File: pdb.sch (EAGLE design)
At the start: 35 parts, among them Q1 20MHz, Q2 IRFR5305PBF, Q3 IRFR5305PBF, U1 TSR_1-2433, U2 LTC2946CMSPBF, U3 LTC2946CMSPBF, U4 LTC2946CMSPBF, U5 ATMEGA48-20AU, U6 TXB0104

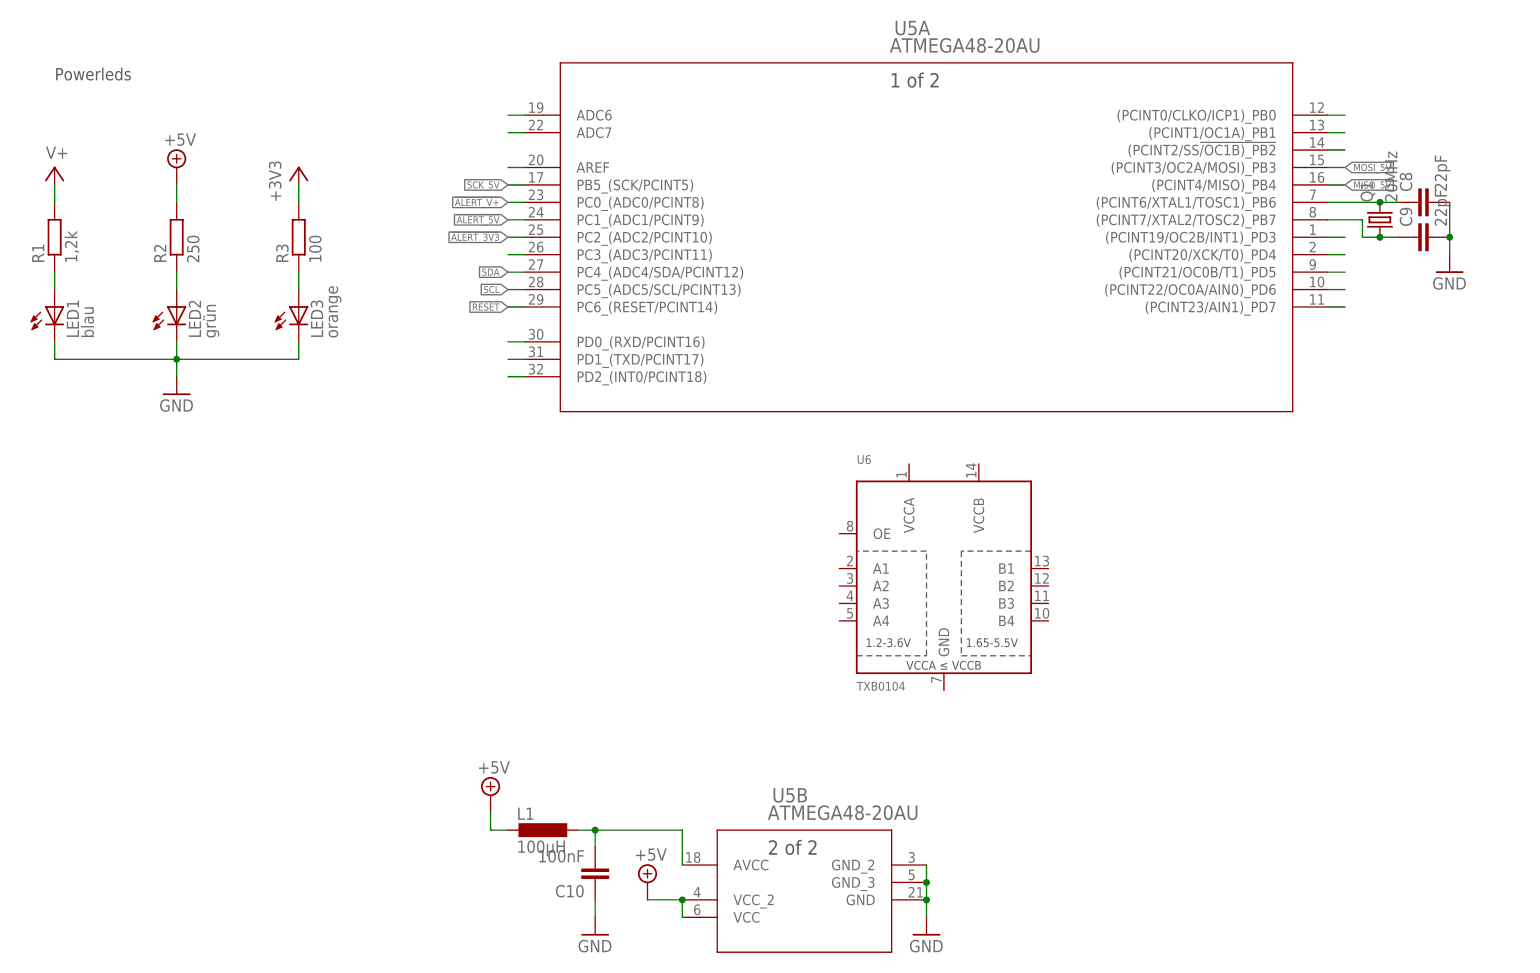
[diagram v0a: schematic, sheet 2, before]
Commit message: Connected Levelshifter
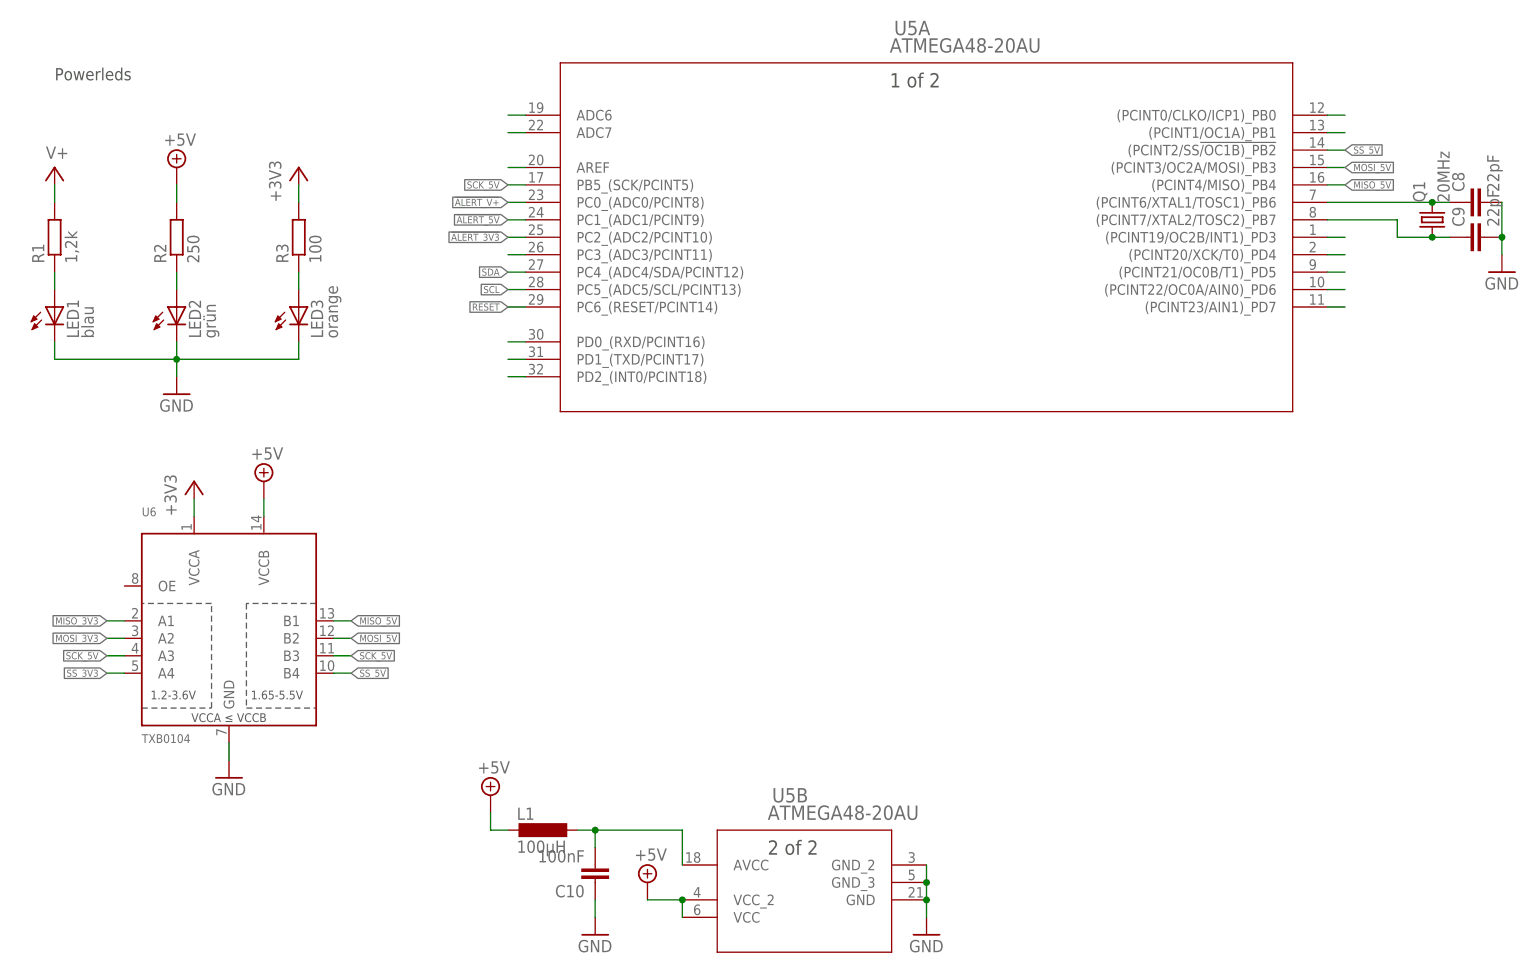
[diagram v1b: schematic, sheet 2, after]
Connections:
- removed net N$24: U5A.(PCINT2/SS!/OC1B)_PB2
- new net MISO_3V3: U6.A1
- new net MOSI_3V3: U6.A2
- new net SS_3V3: U6.A4
- new net SS_5V: U5A.(PCINT2/SS!/OC1B)_PB2, U6.B4
- net +3V3: now also U6.VCCA
- net +5V: now also U6.VCCB
- net GND: now also U6.GND
- net MISO_5V: now also U6.B1
- net MOSI_5V: now also U6.B2
- net SCK_5V: now also U6.A3, U6.B3
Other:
- moved on the sheet: C8, C9, Q1, U6
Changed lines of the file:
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@@
 <part name="SUPPLY15" library="supply2" deviceset="+5V" device=""/>
 <part name="SUPPLY14" library="supply2" deviceset="+5V" device=""/>
+<part name="SUPPLY16" library="supply2" deviceset="+5V" device=""/>
+<part name="GND16" library="supply1" deviceset="GND" device=""/>
+<part name="+3V4" library="supply1" library_urn="urn:adsk.eagle:library:371" deviceset="+3V3" device=""/>
 </parts>
 <sheets>
@@
 <instance part="GND12" gate="1" x="142.24" y="40.64"/>
 <instance part="FRAME2" gate="G$1" x="0" y="0"/>
-<instance part="U6" gate="G$1" x="144.78" y="91.44"/>
-<instance part="Q1" gate="G$1" x="208.28" y="144.78" rot="R90"/>
-<instance part="GND13" gate="1" x="218.44" y="137.16"/>
-<instance part="C8" gate="G$1" x="213.36" y="147.32" rot="R90"/>
-<instance part="C9" gate="G$1" x="213.36" y="142.24" rot="R90"/>
+<instance part="U6" gate="G$1" x="40.64" y="83.82"/>
+<instance part="Q1" gate="G$1" x="215.9" y="144.78" rot="R90"/>
+<instance part="GND13" gate="1" x="226.06" y="137.16"/>
+<instance part="C8" gate="G$1" x="220.98" y="147.32" rot="R90"/>
+<instance part="C9" gate="G$1" x="220.98" y="142.24" rot="R90"/>
 <instance part="C10" gate="G$1" x="93.98" y="48.26" rot="R180"/>
 <instance part="GND14" gate="1" x="93.98" y="40.64"/>
@@
 <instance part="SUPPLY15" gate="+5V" x="78.74" y="60.96"/>
 <instance part="SUPPLY14" gate="+5V" x="101.6" y="48.26"/>
+<instance part="SUPPLY16" gate="+5V" x="45.72" y="106.68"/>
+<instance part="GND16" gate="1" x="40.64" y="63.5"/>
+<instance part="+3V4" gate="G$1" x="35.56" y="106.68"/>
 </instances>
 <busses>
@@
 <pinref part="C9" gate="G$1" pin="2"/>
 <pinref part="GND13" gate="1" pin="GND"/>
-<wire x1="218.44" y1="142.24" x2="218.44" y2="139.7" width="0.1524" layer="91"/>
+<wire x1="226.06" y1="142.24" x2="226.06" y2="139.7" width="0.1524" layer="91"/>
 <pinref part="C8" gate="G$1" pin="2"/>
-<wire x1="218.44" y1="147.32" x2="218.44" y2="142.24" width="0.1524" layer="91"/>
-<junction x="218.44" y="142.24"/>
+<wire x1="226.06" y1="147.32" x2="226.06" y2="142.24" width="0.1524" layer="91"/>
+<junction x="226.06" y="142.24"/>
 </segment>
 <segment>
@@
 <wire x1="93.98" y1="43.18" x2="93.98" y2="45.72" width="0.1524" layer="91"/>
 </segment>
+<segment>
+<pinref part="U6" gate="G$1" pin="GND"/>
+<wire x1="40.64" y1="68.58" x2="40.64" y2="66.04" width="0.1524" layer="91"/>
+<pinref part="GND16" gate="1" pin="GND"/>
+</segment>
 </net>
 <net name="N$4" class="0">
@@
 <pinref part="+3V1" gate="G$1" pin="+3V3"/>
 <wire x1="50.8" y1="149.86" x2="50.8" y2="147.32" width="0.1524" layer="91"/>
+</segment>
+<segment>
+<pinref part="U6" gate="G$1" pin="VCCA"/>
+<wire x1="35.56" y1="101.6" x2="35.56" y2="104.14" width="0.1524" layer="91"/>
+<pinref part="+3V4" gate="G$1" pin="+3V3"/>
 </segment>
 </net>
@@
 <junction x="106.68" y="45.72"/>
 </segment>
+<segment>
+<pinref part="U6" gate="G$1" pin="VCCB"/>
+<wire x1="45.72" y1="101.6" x2="45.72" y2="104.14" width="0.1524" layer="91"/>
+<pinref part="SUPPLY16" gate="+5V" pin="+5V"/>
+</segment>
 </net>
 <net name="V+" class="0">
@@
 <label x="81.28" y="149.86" size="1.016" layer="95" rot="R180" xref="yes"/>
 </segment>
+<segment>
+<pinref part="U6" gate="G$1" pin="A3"/>
+<wire x1="25.4" y1="81.28" x2="22.86" y2="81.28" width="0.1524" layer="91"/>
+<label x="22.86" y="81.28" size="1.016" layer="95" rot="R180" xref="yes"/>
+</segment>
+<segment>
+<pinref part="U6" gate="G$1" pin="B3"/>
+<wire x1="55.88" y1="81.28" x2="58.42" y2="81.28" width="0.1524" layer="91"/>
+<label x="58.42" y="81.28" size="1.016" layer="95" xref="yes"/>
+</segment>
 </net>
 <net name="!ALERT_V+" class="0">
@@
 </segment>
 </net>
-<net name="N$24" class="0">
+<net name="SS_5V" class="0">
 <segment>
 <pinref part="U5" gate="A" pin="(PCINT2/SS!/OC1B)_PB2"/>
 <wire x1="200.66" y1="154.94" x2="203.2" y2="154.94" width="0.1524" layer="91"/>
+<label x="203.2" y="154.94" size="1.016" layer="95" xref="yes"/>
+</segment>
+<segment>
+<pinref part="U6" gate="G$1" pin="B4"/>
+<wire x1="55.88" y1="78.74" x2="58.42" y2="78.74" width="0.1524" layer="91"/>
+<label x="58.42" y="78.74" size="1.016" layer="95" xref="yes"/>
 </segment>
 </net>
@@
 <label x="203.2" y="152.4" size="1.016" layer="95" xref="yes"/>
 </segment>
+<segment>
+<pinref part="U6" gate="G$1" pin="B2"/>
+<wire x1="55.88" y1="83.82" x2="58.42" y2="83.82" width="0.1524" layer="91"/>
+<label x="58.42" y="83.82" size="1.016" layer="95" xref="yes"/>
+</segment>
 </net>
 <net name="MISO_5V" class="0">
@@
 <label x="203.2" y="149.86" size="1.016" layer="95" xref="yes"/>
 </segment>
+<segment>
+<pinref part="U6" gate="G$1" pin="B1"/>
+<wire x1="55.88" y1="86.36" x2="58.42" y2="86.36" width="0.1524" layer="91"/>
+<label x="58.42" y="86.36" size="1.016" layer="95" xref="yes"/>
+</segment>
 </net>
 <net name="N$27" class="0">
@@
 <pinref part="U5" gate="A" pin="(PCINT6/XTAL1/TOSC1)_PB6"/>
 <pinref part="Q1" gate="G$1" pin="2"/>
-<wire x1="200.66" y1="147.32" x2="208.28" y2="147.32" width="0.1524" layer="91"/>
-<wire x1="208.28" y1="147.32" x2="210.82" y2="147.32" width="0.1524" layer="91"/>
-<junction x="208.28" y="147.32"/>
+<wire x1="200.66" y1="147.32" x2="215.9" y2="147.32" width="0.1524" layer="91"/>
+<wire x1="215.9" y1="147.32" x2="218.44" y2="147.32" width="0.1524" layer="91"/>
+<junction x="215.9" y="147.32"/>
 <pinref part="C8" gate="G$1" pin="1"/>
 </segment>
@@
 <segment>
 <pinref part="U5" gate="A" pin="(PCINT7/XTAL2/TOSC2)_PB7"/>
-<wire x1="200.66" y1="144.78" x2="205.74" y2="144.78" width="0.1524" layer="91"/>
-<wire x1="205.74" y1="144.78" x2="205.74" y2="142.24" width="0.1524" layer="91"/>
+<wire x1="200.66" y1="144.78" x2="210.82" y2="144.78" width="0.1524" layer="91"/>
+<wire x1="210.82" y1="144.78" x2="210.82" y2="142.24" width="0.1524" layer="91"/>
 <pinref part="Q1" gate="G$1" pin="1"/>
-<wire x1="205.74" y1="142.24" x2="208.28" y2="142.24" width="0.1524" layer="91"/>
-<wire x1="208.28" y1="142.24" x2="210.82" y2="142.24" width="0.1524" layer="91"/>
-<junction x="208.28" y="142.24"/>
+<wire x1="210.82" y1="142.24" x2="215.9" y2="142.24" width="0.1524" layer="91"/>
+<wire x1="215.9" y1="142.24" x2="218.44" y2="142.24" width="0.1524" layer="91"/>
+<junction x="215.9" y="142.24"/>
 <pinref part="C9" gate="G$1" pin="1"/>
 </segment>
@@
 </segment>
 </net>
+<net name="MISO_3V3" class="0">
+<segment>
+<pinref part="U6" gate="G$1" pin="A1"/>
+<wire x1="25.4" y1="86.36" x2="22.86" y2="86.36" width="0.1524" layer="91"/>
+<label x="22.86" y="86.36" size="1.016" layer="95" rot="R180" xref="yes"/>
+</segment>
+</net>
+<net name="MOSI_3V3" class="0">
+<segment>
+<pinref part="U6" gate="G$1" pin="A2"/>
+<wire x1="25.4" y1="83.82" x2="22.86" y2="83.82" width="0.1524" layer="91"/>
+<label x="22.86" y="83.82" size="1.016" layer="95" rot="R180" xref="yes"/>
+</segment>
+</net>
+<net name="SS_3V3" class="0">
+<segment>
+<pinref part="U6" gate="G$1" pin="A4"/>
+<wire x1="25.4" y1="78.74" x2="22.86" y2="78.74" width="0.1524" layer="91"/>
+<label x="22.86" y="78.74" size="1.016" layer="95" rot="R180" xref="yes"/>
+</segment>
+</net>

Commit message: First parts placed
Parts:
- added ESC: XT60PWFEMALE, amass:XT60PWFEMALE
- added JP1: (no value), pinhead:PINHD-2X8
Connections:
- net GND: now also ESC.-
- net V+: now also ESC.+
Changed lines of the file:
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@@
 <part name="GND16" library="supply1" deviceset="GND" device=""/>
 <part name="+3V4" library="supply1" library_urn="urn:adsk.eagle:library:371" deviceset="+3V3" device=""/>
+<part name="ESC" library="amass" deviceset="XT60PW" device="FEMALE" value="XT60PWFEMALE"/>
+<part name="GND18" library="supply1" deviceset="GND" device=""/>
+<part name="SUPPLY17" library="supply2" library_urn="urn:adsk.eagle:library:372" deviceset="V+" device=""/>
+<part name="JP1" library="pinhead" library_urn="urn:adsk.eagle:library:325" deviceset="PINHD-2X8" device="" package3d_urn="urn:adsk.eagle:package:22481/2"/>
 </parts>
 <sheets>
@@
 <instance part="R6" gate="G$1" x="40.64" y="15.24"/>
 <instance part="FRAME3" gate="G$1" x="-127" y="-50.8"/>
+<instance part="ESC" gate="G$1" x="-99.06" y="-17.78" rot="MR0"/>
+<instance part="GND18" gate="1" x="-86.36" y="-25.4"/>
+<instance part="SUPPLY17" gate="1" x="-86.36" y="-10.16"/>
 </instances>
 <busses>
@@
 <wire x1="2.54" y1="0" x2="2.54" y2="7.62" width="0.1524" layer="91"/>
 </segment>
+<segment>
+<pinref part="ESC" gate="G$1" pin="-"/>
+<wire x1="-88.9" y1="-20.32" x2="-86.36" y2="-20.32" width="0.1524" layer="91"/>
+<wire x1="-86.36" y1="-20.32" x2="-86.36" y2="-22.86" width="0.1524" layer="91"/>
+<pinref part="GND18" gate="1" pin="GND"/>
+</segment>
 </net>
 <net name="V+" class="0">
@@
 <pinref part="SUPPLY3" gate="1" pin="V+"/>
 <wire x1="-22.86" y1="55.88" x2="-22.86" y2="58.42" width="0.1524" layer="91"/>
+</segment>
+<segment>
+<pinref part="ESC" gate="G$1" pin="+"/>
+<wire x1="-88.9" y1="-15.24" x2="-86.36" y2="-15.24" width="0.1524" layer="91"/>
+<pinref part="SUPPLY17" gate="1" pin="V+"/>
+<wire x1="-86.36" y1="-12.7" x2="-86.36" y2="-15.24" width="0.1524" layer="91"/>
 </segment>
 </net>
@@
 <instance part="GND11" gate="1" x="114.3" y="88.9"/>
 <instance part="FRAME1" gate="G$1" x="0" y="0"/>
+<instance part="JP1" gate="A" x="152.4" y="210.82"/>
 </instances>
 <busses>

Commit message: added temperature sensor
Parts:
- added U7: AT30TS74SS8M, jonas_microchip:AT30TS74SS8M
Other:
- note added: "Temperaturmessung"
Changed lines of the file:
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@@
 <part name="SUPPLY17" library="supply2" library_urn="urn:adsk.eagle:library:372" deviceset="V+" device=""/>
 <part name="JP1" library="pinhead" library_urn="urn:adsk.eagle:library:325" deviceset="PINHD-2X8" device="" package3d_urn="urn:adsk.eagle:package:22481/2"/>
+<part name="FRAME4" library="frames" library_urn="urn:adsk.eagle:library:229" deviceset="A3L-LOC" device=""/>
+<part name="U7" library="jonas_microchip" library_urn="urn:adsk.eagle:library:891228" deviceset="AT30TS74" device="SS8M" package3d_urn="urn:adsk.eagle:package:1422804/3"/>
 </parts>
 <sheets>
@@
 </nets>
 </sheet>
+<sheet>
+<plain>
+<text x="109.22" y="165.1" size="2.54" layer="97">Temperaturmessung</text>
+</plain>
+<instances>
+<instance part="FRAME4" gate="G$1" x="0" y="0"/>
+<instance part="U7" gate="IC1" x="124.46" y="142.24"/>
+</instances>
+<busses>
+</busses>
+<nets>
+</nets>
+</sheet>
